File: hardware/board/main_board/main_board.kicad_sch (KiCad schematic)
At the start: 0 parts

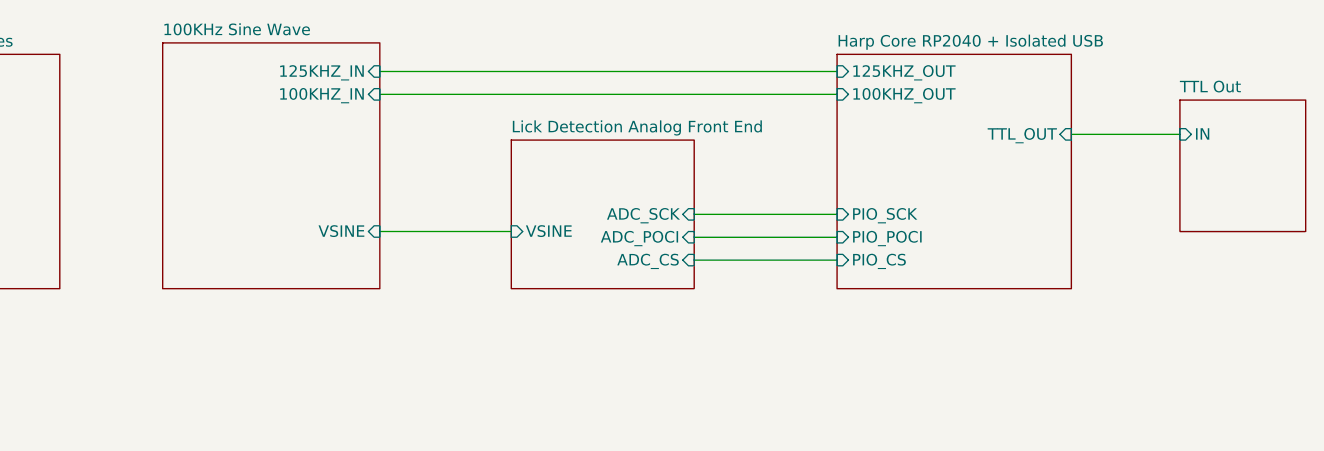
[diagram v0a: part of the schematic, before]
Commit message: split board into two
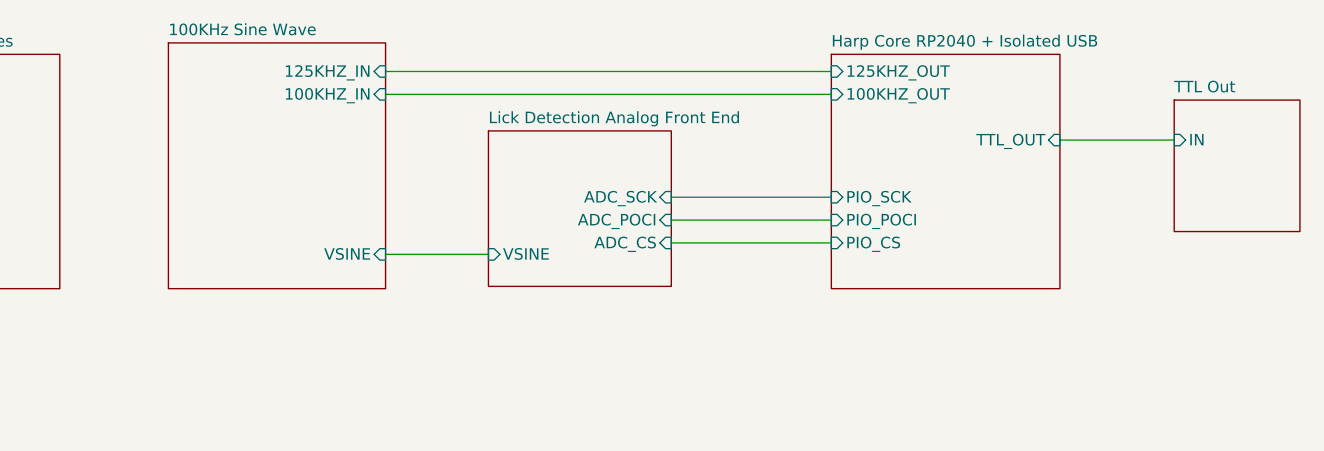
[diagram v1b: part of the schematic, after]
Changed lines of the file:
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@@
 		(title "Lickety Split Capacitive Lick Detector Main Board")
 		(date "2023-09-01")
-		(rev "0.10")
+		(rev "1.0.0")
 		(company "The Allen Institute for Neural Dynamics")
 	)
 	(wire
 		(pts
-			(xy 132.715 91.44) (xy 147.32 91.44)
-		)
-		(stroke
-			(width 0)
-			(type default)
-		)
-	)
-	(wire
-		(pts
-			(xy 167.64 94.615) (xy 183.515 94.615)
-		)
-		(stroke
-			(width 0)
-			(type default)
-		)
-	)
-	(wire
-		(pts
-			(xy 209.55 80.645) (xy 221.615 80.645)
-		)
-		(stroke
-			(width 0)
-			(type default)
-		)
-	)
-	(wire
-		(pts
-			(xy 167.64 92.075) (xy 183.515 92.075)
-		)
-		(stroke
-			(width 0)
-			(type default)
-		)
-	)
-	(wire
-		(pts
-			(xy 132.715 73.66) (xy 183.515 73.66)
-		)
-		(stroke
-			(width 0)
-			(type default)
-		)
-	)
-	(wire
-		(pts
-			(xy 167.64 89.535) (xy 183.515 89.535)
-		)
-		(stroke
-			(width 0)
-			(type default)
-		)
-	)
-	(wire
-		(pts
-			(xy 132.715 76.2) (xy 183.515 76.2)
+			(xy 165.1 92.71) (xy 182.88 92.71)
+		)
+		(stroke
+			(width 0)
+			(type default)
+		)
+	)
+	(wire
+		(pts
+			(xy 165.1 90.17) (xy 182.88 90.17)
+		)
+		(stroke
+			(width 0)
+			(type default)
+		)
+	)
+	(wire
+		(pts
+			(xy 208.28 81.28) (xy 220.98 81.28)
+		)
+		(stroke
+			(width 0)
+			(type default)
+		)
+	)
+	(wire
+		(pts
+			(xy 144.78 93.98) (xy 133.35 93.98)
+		)
+		(stroke
+			(width 0)
+			(type default)
+		)
+	)
+	(wire
+		(pts
+			(xy 133.35 73.66) (xy 182.88 73.66)
+		)
+		(stroke
+			(width 0)
+			(type default)
+		)
+	)
+	(wire
+		(pts
+			(xy 165.1 87.63) (xy 182.88 87.63)
+		)
+		(stroke
+			(width 0)
+			(type default)
+		)
+	)
+	(wire
+		(pts
+			(xy 133.35 76.2) (xy 182.88 76.2)
 		)
 		(stroke
@@
 	)
 	(sheet
-		(at 221.615 76.835)
+		(at 220.98 76.835)
 		(size 13.97 14.605)
 		(fields_autoplaced yes)
@@
 		)
 		(property "Sheetname" "TTL Out"
-			(at 221.615 76.1234 0)
+			(at 220.98 76.1234 0)
 			(effects
 				(font
@@
 		)
 		(property "Sheetfile" "sma_ttl_out.kicad_sch"
-			(at 221.615 92.0246 0)
+			(at 220.98 92.0246 0)
 			(effects
 				(font
@@
 		)
 		(pin "IN" input
-			(at 221.615 80.645 180)
+			(at 220.98 81.28 180)
 			(effects
 				(font
@@
 	)
 	(sheet
-		(at 108.585 70.485)
+		(at 109.22 70.485)
 		(size 24.13 27.305)
 		(fields_autoplaced yes)
@@
 		)
 		(property "Sheetname" "100KHz Sine Wave"
-			(at 108.585 69.7734 0)
+			(at 109.22 69.7734 0)
 			(effects
 				(font
@@
 		)
 		(property "Sheetfile" "function_generator.kicad_sch"
-			(at 108.585 98.3746 0)
+			(at 109.22 98.3746 0)
 			(effects
 				(font
@@
 		)
 		(pin "VSINE" input
-			(at 132.715 91.44 0)
+			(at 133.35 93.98 0)
 			(effects
 				(font
@@
 		)
 		(pin "125KHZ_IN" input
-			(at 132.715 73.66 0)
+			(at 133.35 73.66 0)
 			(effects
 				(font
@@
 		)
 		(pin "100KHZ_IN" input
-			(at 132.715 76.2 0)
+			(at 133.35 76.2 0)
 			(effects
 				(font
@@
 	)
 	(sheet
-		(at 147.32 81.28)
-		(size 20.32 16.51)
+		(at 144.78 80.264)
+		(size 20.32 17.272)
 		(fields_autoplaced yes)
 		(stroke
@@
 		)
 		(property "Sheetname" "Lick Detection Analog Front End"
-			(at 147.32 80.5684 0)
+			(at 144.78 79.5524 0)
 			(effects
 				(font
@@
 		)
 		(property "Sheetfile" "lick_detection_afe.kicad_sch"
-			(at 147.32 98.3746 0)
+			(at 144.78 98.1206 0)
 			(effects
 				(font
@@
 		)
 		(pin "VSINE" input
-			(at 147.32 91.44 180)
+			(at 144.78 93.98 180)
 			(effects
 				(font
@@
 		)
 		(pin "ADC_SCK" input
-			(at 167.64 89.535 0)
+			(at 165.1 87.63 0)
 			(effects
 				(font
@@
 		)
 		(pin "ADC_CS" input
-			(at 167.64 94.615 0)
+			(at 165.1 92.71 0)
 			(effects
 				(font
@@
 		)
 		(pin "ADC_POCI" input
-			(at 167.64 92.075 0)
+			(at 165.1 90.17 0)
 			(effects
 				(font
@@
 	)
 	(sheet
-		(at 183.515 71.755)
-		(size 26.035 26.035)
+		(at 182.88 71.755)
+		(size 25.4 26.035)
 		(fields_autoplaced yes)
 		(stroke
@@
 		)
 		(property "Sheetname" "Harp Core RP2040 + Isolated USB"
-			(at 183.515 71.0434 0)
+			(at 182.88 71.0434 0)
 			(effects
 				(font
@@
 		)
 		(property "Sheetfile" "isolated_usb_rp2040.kicad_sch"
-			(at 183.515 98.3746 0)
+			(at 182.88 98.3746 0)
 			(effects
 				(font
@@
 		)
 		(pin "TTL_OUT" input
-			(at 209.55 80.645 0)
+			(at 208.28 81.28 0)
 			(effects
 				(font
@@
 		)
 		(pin "PIO_SCK" input
-			(at 183.515 89.535 180)
+			(at 182.88 87.63 180)
 			(effects
 				(font
@@
 		)
 		(pin "PIO_POCI" input
-			(at 183.515 92.075 180)
+			(at 182.88 90.17 180)
 			(effects
 				(font
@@
 		)
 		(pin "PIO_CS" input
-			(at 183.515 94.615 180)
+			(at 182.88 92.71 180)
 			(effects
 				(font
@@
 		)
 		(pin "100KHZ_OUT" input
-			(at 183.515 76.2 180)
+			(at 182.88 76.2 180)
 			(effects
 				(font
@@
 		)
 		(pin "125KHZ_OUT" input
-			(at 183.515 73.66 180)
-			(effects
-				(font
+			(at 182.88 73.66 180)
+			(effects
+				(font
